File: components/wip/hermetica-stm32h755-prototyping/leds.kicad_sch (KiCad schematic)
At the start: 46 parts, among them J28 Conn_01x01, J29 Conn_01x01, J3 Conn_01x01, J46 Conn_01x01, J51 Conn_01x01, J52 Conn_01x01, J9 Conn_01x01, Q1 DIODESINC-MMBT4401-7-F-SOT-23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, Q2 DIODESINC-MMBT4401-7-F-SOT-23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, Q3 DIODESINC-MMBT4401-7-F-SOT-23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, Q4 DIODESINC-MMBT4401-7-F-SOT-23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, Q5 DIODESINC-MMBT4401-7-F-SOT-23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, Q6 DIODESINC-MMBT4401-7-F-SOT-23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, Q7 DIODESINC-MMBT4401-7-F-SOT-23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

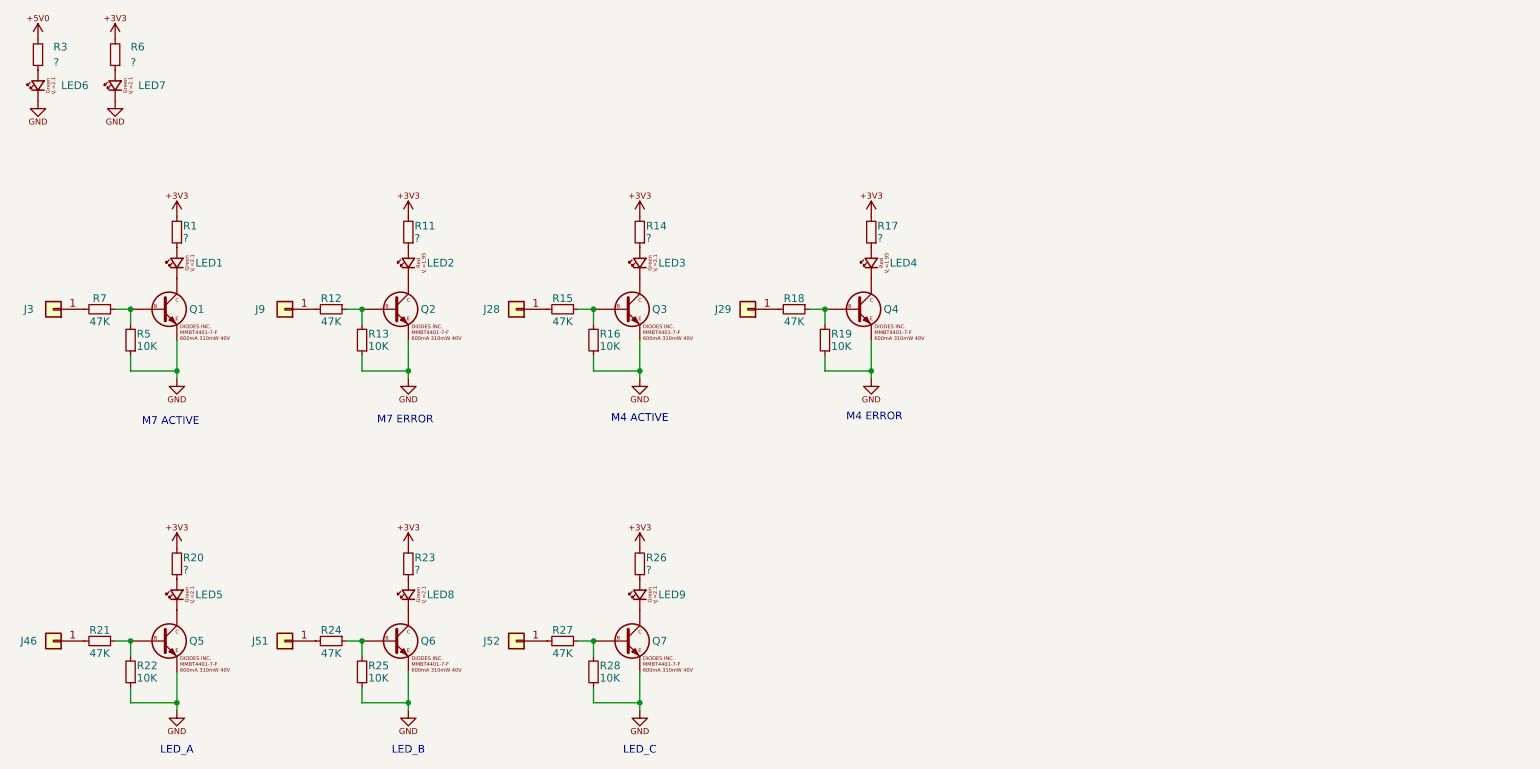
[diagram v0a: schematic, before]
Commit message: STM32H755ZIT6 dev board
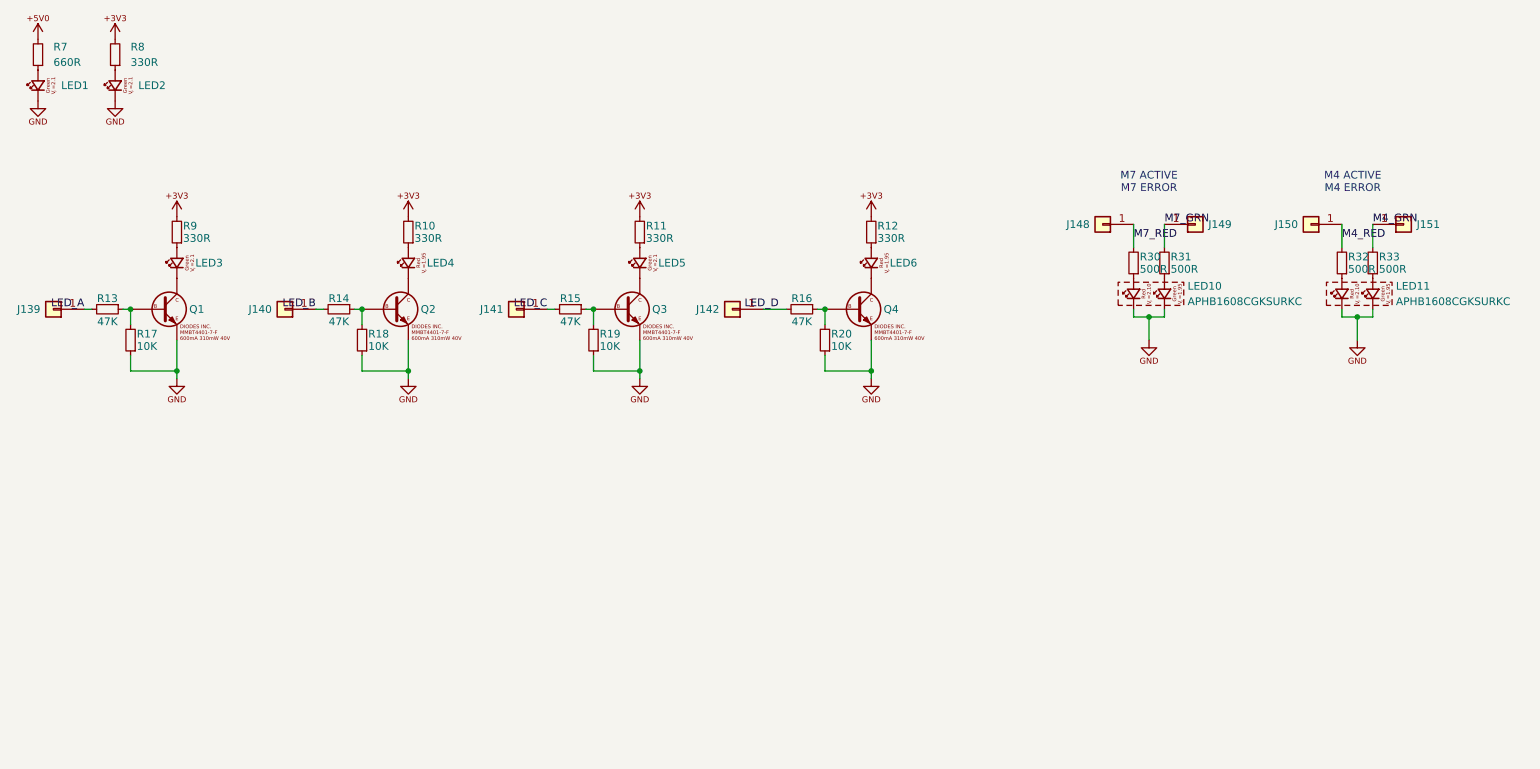
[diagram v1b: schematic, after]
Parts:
- removed J46, J51, J52: Conn_01x01, djStandard:CONNECTOR-PCB-HANDSOLDER-01X01-FEMALE, symbol Connector_Generic:Conn_01x01
- removed LED5, LED8, LED9: KINGBRIGHT-LED-0402-ORANGE, djStandard:KINGBRIGHT-LED-APHHS1005-0402, symbol DJ:KINGBRIGHT-LED-0402-GREEN
- removed Q5, Q6, Q7: DIODESINC-MMBT4401-7-F-SOT-23-3, Package_TO_SOT_SMD:SOT-23-3, symbol DJ:DIODESINC-MMBT4401-7-F-SOT-23-3
- removed R20, R23, R26: ?, djStandard:R_0402_1005Metric, symbol DJ:R
- removed R21, R24, R27: 47K, djStandard:R_0402_1005Metric, symbol DJ:R
- removed R22, R25, R28: 10K, djStandard:R_0402_1005Metric, symbol DJ:R
- added J148, J149, J150, J151: Conn_01x01, djStandard:CONNECTOR-PCB-HANDSOLDER-01X01-FEMALE, symbol Connector_Generic:Conn_01x01
- added LED10, LED11: APHB1608CGKSURKC, djStandard:KINGBRIGHT-APHB1608CGKSURKC, symbol DJ:KINGBRIGHT-LED-0603-GREEN/RED
- added R30, R31, R32, R33: 500R, djStandard:R_0402_1005Metric, symbol DJ:R
- R10: renamed from R11; value ? -> 330R
- R11: renamed from R14; value ? -> 330R
- R12: renamed from R17; value ? -> 330R
- R7: renamed from R3; value ? -> 660R
- R8: renamed from R6; value ? -> 330R
- R9: renamed from R1; value ? -> 330R
- renumbered J3 to J139, J9 to J140, J28 to J141, J29 to J142, LED6 to LED1, LED7 to LED2, LED1 to LED3, LED2 to LED4, LED3 to LED5, LED4 to LED6, R7 to R13, R12 to R14, R18 to R16, R5 to R17, R13 to R18, R16 to R19, R19 to R20
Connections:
- net GND: now also LED10.2 (K_GREEN), LED10.4 (K_RED), LED11.2 (K_GREEN), LED11.4 (K_RED)
- net LED_B: now reaches J140.1 (Pin_1), R14.2
- net LED_C: now reaches J141.1 (Pin_1), R15.2
- net LED_A: now reaches J139.1 (Pin_1), R13.2
- net LED_D: now reaches J142.1 (Pin_1), R16.2
- new net: LED11.1 (A_GREEN), R33.1
- new net: LED10.1 (A_GREEN), R31.1
- new net: LED10.3 (A_RED), R30.1
- new net: LED11.3 (A_RED), R32.1
- new net M4_GRN: J151.1 (Pin_1), R33.2
- new net M4_RED: J150.1 (Pin_1), R32.2
- new net M7_GRN: J149.1 (Pin_1), R31.2
- new net M7_RED: J148.1 (Pin_1), R30.2
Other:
- note added: "M4 ACTIVE M4 ERROR"
- note added: "M7 ACTIVE M7 ERROR"
- note removed: "LED_A"
- note removed: "LED_B"
- note removed: "LED_C"
- note removed: "M4 ACTIVE"
- note removed: "M4 ERROR"
- note removed: "M7 ACTIVE"
- note removed: "M7 ERROR"
- moved on the sheet: J142, R13, R14, R15, R16
